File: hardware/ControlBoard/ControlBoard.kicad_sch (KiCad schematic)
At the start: 144 parts, among them J1 Lamp 1 Out, J10 CAN, J2 ESTOP1, J20 SWD, J3 ESTOP2, J4 Lamp 3 Out, J5 Lamp 2 Out, J6 Lamp 4 Out, J7 PWR_IN, Q1 2N7002, Q2 2N7002, Q3 2N7002, Q4 2N7002, SW1 RST, U3 AMS1117, U4 MCP1804x-3302xMT, U7 SN65HVD232, U9 STM32F334R8Tx

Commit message: Finish (?) micro stuff, define components, add UART header
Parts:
- removed C18: 10nF, Capacitor_SMD:C_0603_1608Metric, symbol Device:C_Small
- removed C?: 1uF, Capacitor_SMD:C_0805_2012Metric, symbol Device:C_Small
- removed C?: 10uF, Capacitor_SMD:C_0805_2012Metric, symbol Device:C_Small
- removed D? (x6): ESD9B3.3ST5G, Diode_SMD:D_SOD-923, symbol Diode:ESD9B3.3ST5G
- removed J20: SWD, Connector_PinSocket_1.27mm:PinSocket_2x03_P1.27mm_Vertical, symbol Connector_Generic:Conn_02x03_Odd_Even
- removed PA15, PA7, PB3, PB4, PB5, PB7, TP7, TP8: TestPoint, TestPoint:TestPoint_Pad_D1.0mm, symbol Connector:TestPoint
- removed R49, R50: 1k, Resistor_SMD:R_0603_1608Metric, symbol Device:R_Small
- removed R?: 10k, Resistor_SMD:R_0805_2012Metric, symbol Device:R_Small
- removed R?: 22.1k, Resistor_SMD:R_0805_2012Metric, symbol Device:R_Small
- removed R?: 1k, Resistor_SMD:R_0805_2012Metric, symbol Device:R_Small
- removed R?: 47.5k, Resistor_SMD:R_0805_2012Metric, symbol Device:R_Small
- removed SW1: RST, Button_Switch_SMD:SW_SPST_B3U-1100P, symbol Switch:SW_SPST
- removed U9: STM32F334R8Tx, Package_QFP:LQFP-64_10x10mm_P0.5mm, symbol MCU_ST_STM32F3:STM32F334R8Tx
- removed U?: CP2102-GM, controlLib:CP2102-GM, symbol CP2102-GM:CP2102-GM
- added D1, D10, D4, D6, D7, D8: SMAJ5.0CA, Diode_SMD:D_SMA, symbol Device:D_TVS
- added J13: AVAILABLE GPIO, Connector_PinHeader_2.54mm:PinHeader_1x09_P2.54mm_Vertical, symbol Connector_Generic:Conn_01x09
- added J9: UART BACKUP, Connector_PinHeader_2.54mm:PinHeader_1x04_P2.54mm_Vertical, symbol Connector_Generic:Conn_01x04
- D5, D9: renamed from D?; Digikey (none) -> 1N5819HW-FDICT-ND
- Q5, Q6: renamed from Q?; Digikey (none) -> 641-1790-1-ND
- gave numbers to parts that had none: 63
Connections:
- net +3V3: now also J9.1 (Pin_1)
- net CAN_RX: now also U5.25 (IO48); no longer U5.21 (IO13)
- net CAN_TX: now also U5.26 (IO45); no longer U5.22 (IO14)
- net GND: now also D1.2 (A2), D10.2 (A2), D4.2 (A2), D6.2 (A2), D7.2 (A2), D8.2 (A2), J9.4 (Pin_4)
- net LAMP1_ON: now also U5.4 (IO4); no longer U5.15 (IO3)
- net LAMP2_ON: now also U5.5 (IO5); no longer U5.16 (IO46)
- net LAMP3_ON: now also U5.28 (IO35); no longer U5.17 (IO9)
- net LAMP4_ON: now also U5.15 (IO3); no longer U5.18 (IO10)
- net U0RXD: now also J9.3 (Pin_3)
- net U0TXD: now also J9.2 (Pin_2)
- net USB_D+: now also D8.1 (A1)
- net USB_D-: now also D10.1 (A1)
- net USB_DN: now also D6.1 (A1)
- net USB_DP: now also D4.1 (A1)
- net VBUS: now also D1.1 (A1)
- net VBUSB: now also D7.1 (A1)
- net GPIO11: now reaches U5.19 (IO11)
- net GPIO11: now also J13.4 (Pin_4)
- net GPIO12: now reaches U5.20 (IO12)
- net GPIO12: now also J13.5 (Pin_5)
- net GPIO21: now reaches U5.23 (IO21)
- net GPIO21: now also J13.8 (Pin_8)
- net GPIO47: now reaches U5.24 (IO47)
- net GPIO47: now also J13.9 (Pin_9)
- new net GPIO10: J13.3 (Pin_3), U5.18 (IO10)
- new net GPIO13: J13.6 (Pin_6), U5.21 (IO13)
- new net GPIO14: J13.7 (Pin_7), U5.22 (IO14)
- new net GPIO46: J13.1 (Pin_1), U5.16 (IO46)
- new net GPIO9: J13.2 (Pin_2), U5.17 (IO9)
- no-connect marks 23 -> 21
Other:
- note added: "IDK WHAT THESE ARE FOR - MAYBE LEFTOVER FROM STM32?"
- note added: "MCU STUFF"
- note added: "POWER"
- note removed: "Any reason for using these diodes? Would opt to use ones from dev board"
- note removed: "ESP USB:"
- note removed: "ESP32"
- note removed: "MCU MISC"
- note removed: "POWER CONVERTERS"
- note removed: "Power Intake"
- note removed: "STM32 (remove after ESP32 is verified)"
- note removed: "Same - any reason for using these transistors? Would opt to use ones from dev board"
- note removed: "Sense Resistor: I_limit = 47mV/Rsense FB Pin: Compared against 1.233V reference to pull PWRGOOD high Timer Pin: dv * (C/i) = dt 64nF capacitor is 1ms allowed charge time"
- note removed: "are these necessary?"
- moved on the sheet: C1, C10, C11, C12, C13, C14, C15, C16, C17, C19, C2, C20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

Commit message: Control Board Power Changes
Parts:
- removed C19, C20, C21, C22, C23, C24: 0.1uF, Capacitor_SMD:C_0805_2012Metric, symbol Device:C_Small
- removed C4, C8: 1uF, Capacitor_SMD:C_1206_3216Metric, symbol Device:C_Small
- removed C5: 22uF, Capacitor_SMD:C_1206_3216Metric, symbol Device:C_Small
- removed C7: 22uF, Capacitor_SMD:C_1206_3216Metric_Pad1.33x1.80mm_HandSolder, symbol Device:C_Small
- removed J16: Conn_01x02_MountingPin, Connector_PinHeader_2.54mm:PinHeader_1x02_P2.54mm_Horizontal, symbol Connector_Generic_MountingPin:Conn_01x02_MountingPin
- removed U3: AMS1117, SOT229P700X180-4N, symbol 3v3LDO:AMS1117
- removed U4: MCP1804x-3302xMT, Package_TO_SOT_SMD:SOT-89-5, symbol Regulator_Linear:MCP1804x-3302xMT
- added C?: 1u, symbol Device:C_Small
- added C?: 2.2u, symbol Device:C_Small
- added C?: 0.1u, symbol Device:C_Small
- added C?: 100n, symbol Device:C_Small
- added C? (x2): 22u, symbol Device:C_Small
- added C?: 100p, symbol Device:C_Small
- added C?: 10u, symbol Device:C_Small
- added L?: 3.9u, symbol Device:L_Small
- added U?: AP63203WU, controlLib:AP63203WU-7, symbol Regulator_Switching:AP63203WU
- added U?: AP2210K-5.0TRG1, controlLib:AP2210K-5.0TRG1, symbol controlLib:AP2210K-5.0TRG1
- C3: value 10u -> 4.7u
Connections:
- net +12V: now also C?.2, C?.2, U?.1 (VIN), U?.2 (EN), U?.3 (EN), U?.3 (IN)
- net +3V3: now also C?.1, C?.1, C?.1, L?.2, U?.1 (FB)
- net +5V: now also C?.1, U?.5 (VOUT); no longer C10.2, C2.2, D5.1 (K), D9.1 (K)
- net GND: now also C?.1, C?.1, C?.2, C?.2, C?.2, C?.2, C?.2, U?.2 (GND), U?.4 (GND)
- new net: C10.2, D9.1 (K)
- new net: C?.2, L?.1, U?.5 (SW)
- new net: C?.1, U?.6 (BST)
- new net: C?.1, U?.4 (BYP)
- new net: C2.2, D5.1 (K)
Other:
- note added: "REVIEW V0.01"
- note removed: "IDK WHAT THESE ARE FOR - MAYBE LEFTOVER FROM STM32?"
- note removed: "VERIFY LOADING ON CONVERTERS AFTER DESIGN DONE"
- note removed: "What's this for?"

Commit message: Add note
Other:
- note added: "These IO are next to eachother on the chip"
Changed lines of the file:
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@@
+    (effects (font (size 1.27 1.27)) (justify left bottom))
+  )
+  (text "These IO are next to eachother on the chip" (at 248.92 275.59 0)
     (effects (font (size 1.27 1.27)) (justify left bottom))
   )

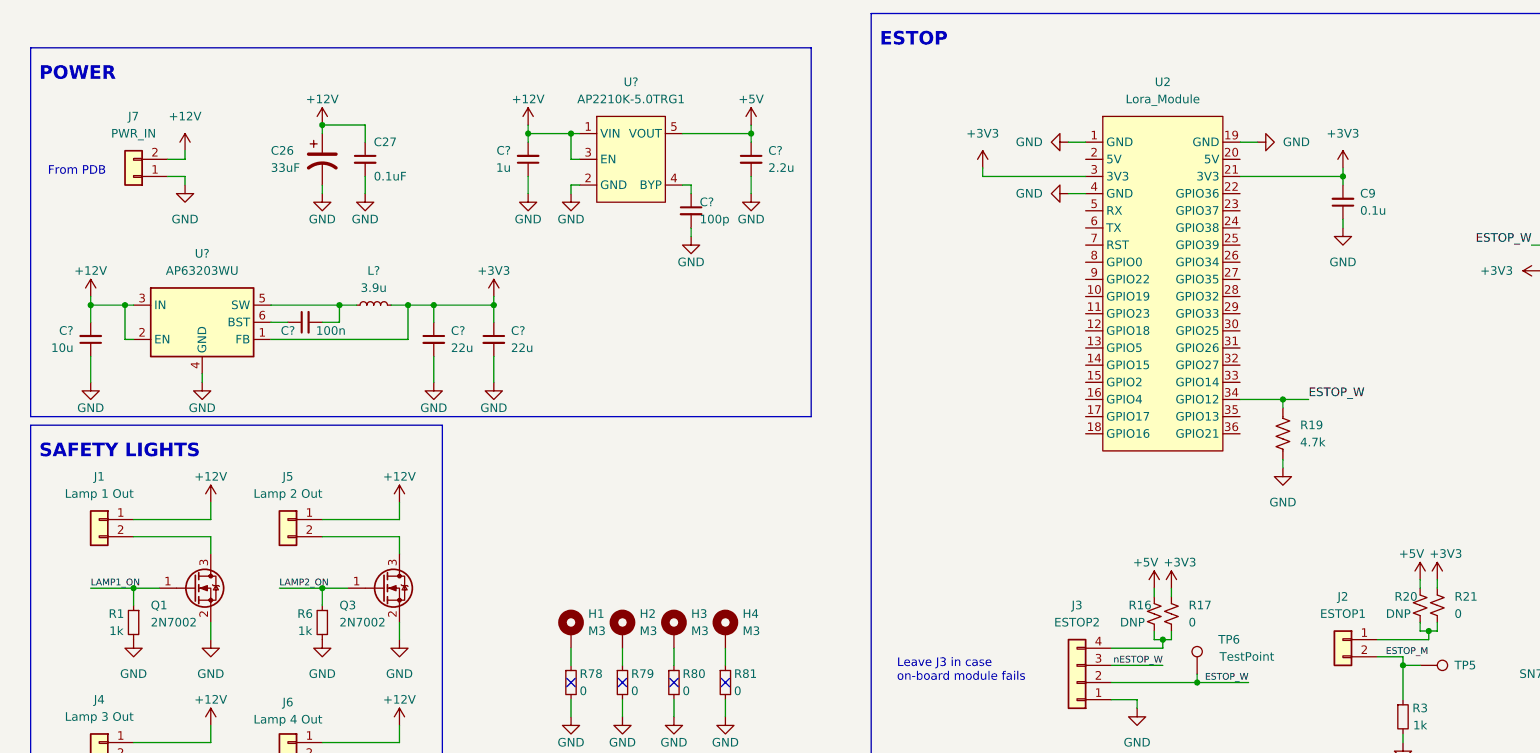
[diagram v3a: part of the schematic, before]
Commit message: Fix Regulators, Change LORA Module Supply
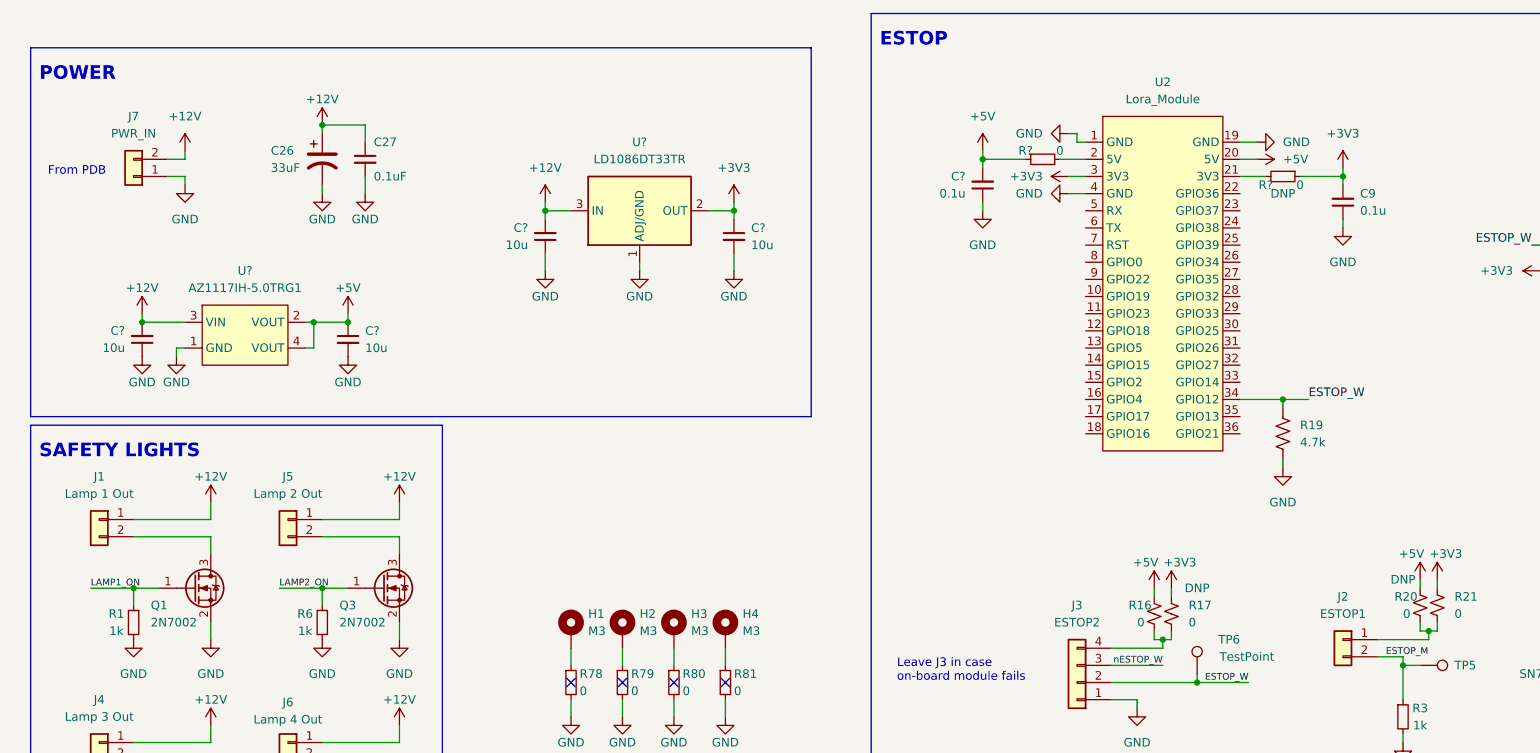
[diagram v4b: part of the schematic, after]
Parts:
- removed C?: 1u, symbol Device:C_Small
- removed C?: 2.2u, symbol Device:C_Small
- removed C?: 100n, symbol Device:C_Small
- removed C? (x2): 22u, symbol Device:C_Small
- removed C?: 100p, symbol Device:C_Small
- removed C?: 10u, symbol Device:C_Small
- removed L?: 3.9u, symbol Device:L_Small
- removed U?: AP63203WU, controlLib:AP63203WU-7, symbol Regulator_Switching:AP63203WU
- removed U?: AP2210K-5.0TRG1, controlLib:AP2210K-5.0TRG1, symbol controlLib:AP2210K-5.0TRG1
- added C?: 0.1u, symbol Device:C_Small
- added C? (x4): 10u, symbol Device:C_Small
- added R? (x2): 0, symbol Device:R_Small
- added U?: LD1086DT33TR, controlLib:LD1086DT33TR, symbol Regulator_Linear:LD1086DT33TR
- added U?: AZ1117IH-5.0TRG1, controlLib:AZ1117IH-5.0TRG1, symbol controlLib:AZ1117IH-5.0TRG1
- R16: value DNP -> 0
- R17: DNP (none) -> DNP
- R20: value DNP -> 0; DNP (none) -> DNP
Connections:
- net +12V: now also C?.2, C?.2, U?.3 (IN), U?.3 (VIN)
- net +3V3: now also C?.1, R?.1, U?.2 (OUT); no longer U2.21 (3V3)
- net +5V: now also U2.20 (5V), C?.1, C?.2, R?.1, U?.2 (VOUT), U?.4 (VOUT)
- net GND: now also C?.1, C?.1, C?.1, C?.2, C?.2, U?.1 (ADJ/GND), U?.1 (GND)
- net at U2.2 (5V): now also R?.2
- new net: R?.2, U2.21 (3V3)
